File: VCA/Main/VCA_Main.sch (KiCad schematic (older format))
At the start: 35 parts, among them J1 Power, J10 IO_B, J11 IO_Power, J5 IO_A, U1 AS3360, U2 TL072, U3 TL072, U4 TL072

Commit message: Clean up VCA boards
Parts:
- added C4, C5: C, Capacitor_SMD:C_0805_2012Metric, symbol Device:C
- added R25, R26, R27, R28: R_US, Resistor_SMD:R_0805_2012Metric, symbol Device:R_US
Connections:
- net Out_A: now also R27.1, R28.1; no longer U4.1, U4.2 (-)
- net Out_B: now also R25.1, R26.1; no longer U4.6 (-), U4.7
- new net: C5.1, R27.2, U4.1
- new net: C5.2, R28.2, U4.2 (-)
- new net: C4.1, R25.2, U4.7
- new net: C4.2, R26.2, U4.6 (-)
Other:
- moved on the sheet: J1, J10, J11, J5

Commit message: Bunch of bug fixes and tweaks
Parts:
- added C6, C7, C8, C9: C, Capacitor_SMD:C_0805_2012Metric, symbol Device:C
- added H1: Top_MH1, Eurorack:eurorack_mounting_hole, symbol Mechanical:MountingHole_Pad
- added H2: Bottom_MH1, Eurorack:eurorack_mounting_hole, symbol Mechanical:MountingHole_Pad
- added H3: Top_MH2, Eurorack:eurorack_mounting_hole, symbol Mechanical:MountingHole_Pad
- added H4: Bottom_MH2, Eurorack:eurorack_mounting_hole, symbol Mechanical:MountingHole_Pad
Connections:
- net -12V: no longer J11.3 (Pin_3)
- net GNDREF: now also H1.1, H2.1, H3.1, H4.1
- net at R10.2, R8.1, U3.1: now also C7.1
- net at R4.1, R5.1, R6.1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: now also C7.2
- net at R10.1, R12.2, U3.6 (-): now also C9.2
- net at R12.1, R15.1, U3.7: now also C9.1
- net at R7.1, R9.2, U2.1: now also C6.1
- net at R1.1, R2.1, R3.1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: now also C6.2
- net at R11.2, R9.1, U2.6 (-): now also C8.2
- net at R11.1, R13.1, U2.7: now also C8.1
- no-connect marks 0 -> 1
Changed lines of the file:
@@
 	10500 3550 10600 3550
-Wire Wire Line
-	10550 2950 10250 2950
-Wire Wire Line
-	10250 2950 10250 3250
-$Comp
-L power:-12V #PWR0105
-U 1 1 5D8742CF
-P 10250 3250
-F 0 "#PWR0105" H 10250 3350 50  0001 C CNN
-F 1 "-12V" H 10265 3423 50  0000 C CNN
-F 2 "" H 10250 3250 50  0001 C CNN
-F 3 "" H 10250 3250 50  0001 C CNN
-	1    10250 3250
-	-1   0    0    1
-$EndComp
 Wire Wire Line
 	9750 5150 10600 5150
@@
 	8700 5500 8800 5500
 Connection ~ 8700 5500
+$Comp
+L Device:C C6
+U 1 1 5D936AAB
+P 2400 2450
+F 0 "C6" V 2148 2450 50  0000 C CNN
+F 1 "C" V 2239 2450 50  0000 C CNN
+F 2 "Capacitor_SMD:C_0805_2012Metric" H 2438 2300 50  0001 C CNN
+F 3 "~" H 2400 2450 50  0001 C CNN
+	1    2400 2450
+	0    1    1    0
+$EndComp
+Wire Wire Line
+	2550 2450 2800 2450
+Wire Wire Line
+	2800 2450 2800 2000
+Connection ~ 2800 2000
+Wire Wire Line
+	2250 2450 2000 2450
+Wire Wire Line
+	2000 2450 2000 2000
+Connection ~ 2000 2000
+$Comp
+L Device:C C8
+U 1 1 5D94AAF9
+P 3700 2350
+F 0 "C8" V 3448 2350 50  0000 C CNN
+F 1 "C" V 3539 2350 50  0000 C CNN
+F 2 "Capacitor_SMD:C_0805_2012Metric" H 3738 2200 50  0001 C CNN
+F 3 "~" H 3700 2350 50  0001 C CNN
+	1    3700 2350
+	0    1    1    0
+$EndComp
+Wire Wire Line
+	3550 2350 3300 2350
+Wire Wire Line
+	3300 2350 3300 1900
+Connection ~ 3300 1900
+Wire Wire Line
+	3850 2350 4100 2350
+Wire Wire Line
+	4100 2350 4100 1900
+Connection ~ 4100 1900
+$Comp
+L Device:C C7
+U 1 1 5D960DB1
+P 2400 5550
+F 0 "C7" V 2148 5550 50  0000 C CNN
+F 1 "C" V 2239 5550 50  0000 C CNN
+F 2 "Capacitor_SMD:C_0805_2012Metric" H 2438 5400 50  0001 C CNN
+F 3 "~" H 2400 5550 50  0001 C CNN
+	1    2400 5550
+	0    1    1    0
+$EndComp
+Wire Wire Line
+	2000 5100 2000 5550
+Wire Wire Line
+	2000 5550 2250 5550
+Connection ~ 2000 5100
+Wire Wire Line
+	2800 5100 2800 5550
+Wire Wire Line
+	2800 5550 2550 5550
+Connection ~ 2800 5100
+$Comp
+L Device:C C9
+U 1 1 5D9785AA
+P 3700 5450
+F 0 "C9" V 3448 5450 50  0000 C CNN
+F 1 "C" V 3539 5450 50  0000 C CNN
+F 2 "Capacitor_SMD:C_0805_2012Metric" H 3738 5300 50  0001 C CNN
+F 3 "~" H 3700 5450 50  0001 C CNN
+	1    3700 5450
+	0    1    1    0
+$EndComp
+Wire Wire Line
+	3300 5000 3300 5450
+Wire Wire Line
+	3300 5450 3550 5450
+Connection ~ 3300 5000
+Wire Wire Line
+	3850 5450 4100 5450
+Wire Wire Line
+	4100 5450 4100 5000
+Connection ~ 4100 5000
+$Comp
+L Mechanical:MountingHole_Pad H1
+U 1 1 5D996C4A
+P 7650 800
+F 0 "H1" H 7750 849 50  0000 L CNN
+F 1 "Top_MH1" H 7750 758 50  0000 L CNN
+F 2 "Eurorack:eurorack_mounting_hole" H 7650 800 50  0001 C CNN
+F 3 "~" H 7650 800 50  0001 C CNN
+	1    7650 800
+	1    0    0    -1
+$EndComp
+$Comp
+L power:GNDREF #PWR0133
+U 1 1 5D997D60
+P 7650 900
+F 0 "#PWR0133" H 7650 650 50  0001 C CNN
+F 1 "GNDREF" H 7655 727 50  0001 C CNN
+F 2 "" H 7650 900 50  0001 C CNN
+F 3 "" H 7650 900 50  0001 C CNN
+	1    7650 900
+	1    0    0    -1
+$EndComp
+$Comp
+L Mechanical:MountingHole_Pad H3
+U 1 1 5D999222
+P 8500 800
+F 0 "H3" H 8600 849 50  0000 L CNN
+F 1 "Top_MH2" H 8600 758 50  0000 L CNN
+F 2 "Eurorack:eurorack_mounting_hole" H 8500 800 50  0001 C CNN
+F 3 "~" H 8500 800 50  0001 C CNN
+	1    8500 800
+	1    0    0    -1
+$EndComp
+$Comp
+L power:GNDREF #PWR0134
+U 1 1 5D999228
+P 8500 900
+F 0 "#PWR0134" H 8500 650 50  0001 C CNN
+F 1 "GNDREF" H 8505 727 50  0001 C CNN
+F 2 "" H 8500 900 50  0001 C CNN
+F 3 "" H 8500 900 50  0001 C CNN
+	1    8500 900
+	1    0    0    -1
+$EndComp
+$Comp
+L Mechanical:MountingHole_Pad H2
+U 1 1 5D9A4134
+P 7650 1200
+F 0 "H2" H 7750 1249 50  0000 L CNN
+F 1 "Bottom_MH1" H 7750 1158 50  0000 L CNN
+F 2 "Eurorack:eurorack_mounting_hole" H 7650 1200 50  0001 C CNN
+F 3 "~" H 7650 1200 50  0001 C CNN
+	1    7650 1200
+	1    0    0    -1
+$EndComp
+$Comp
+L power:GNDREF #PWR0135
+U 1 1 5D9A413A
+P 7650 1300
+F 0 "#PWR0135" H 7650 1050 50  0001 C CNN
+F 1 "GNDREF" H 7655 1127 50  0001 C CNN
+F 2 "" H 7650 1300 50  0001 C CNN
+F 3 "" H 7650 1300 50  0001 C CNN
+	1    7650 1300
+	1    0    0    -1
+$EndComp
+$Comp
+L Mechanical:MountingHole_Pad H4
+U 1 1 5D9AEFCE
+P 8500 1200
+F 0 "H4" H 8600 1249 50  0000 L CNN
+F 1 "Bottom_MH2" H 8600 1158 50  0000 L CNN
+F 2 "Eurorack:eurorack_mounting_hole" H 8500 1200 50  0001 C CNN
+F 3 "~" H 8500 1200 50  0001 C CNN
+	1    8500 1200
+	1    0    0    -1
+$EndComp
+$Comp
+L power:GNDREF #PWR0136
+U 1 1 5D9AEFD4
+P 8500 1300
+F 0 "#PWR0136" H 8500 1050 50  0001 C CNN
+F 1 "GNDREF" H 8505 1127 50  0001 C CNN
+F 2 "" H 8500 1300 50  0001 C CNN
+F 3 "" H 8500 1300 50  0001 C CNN
+	1    8500 1300
+	1    0    0    -1
+$EndComp
+NoConn ~ 10550 2950
 $EndSCHEMATC

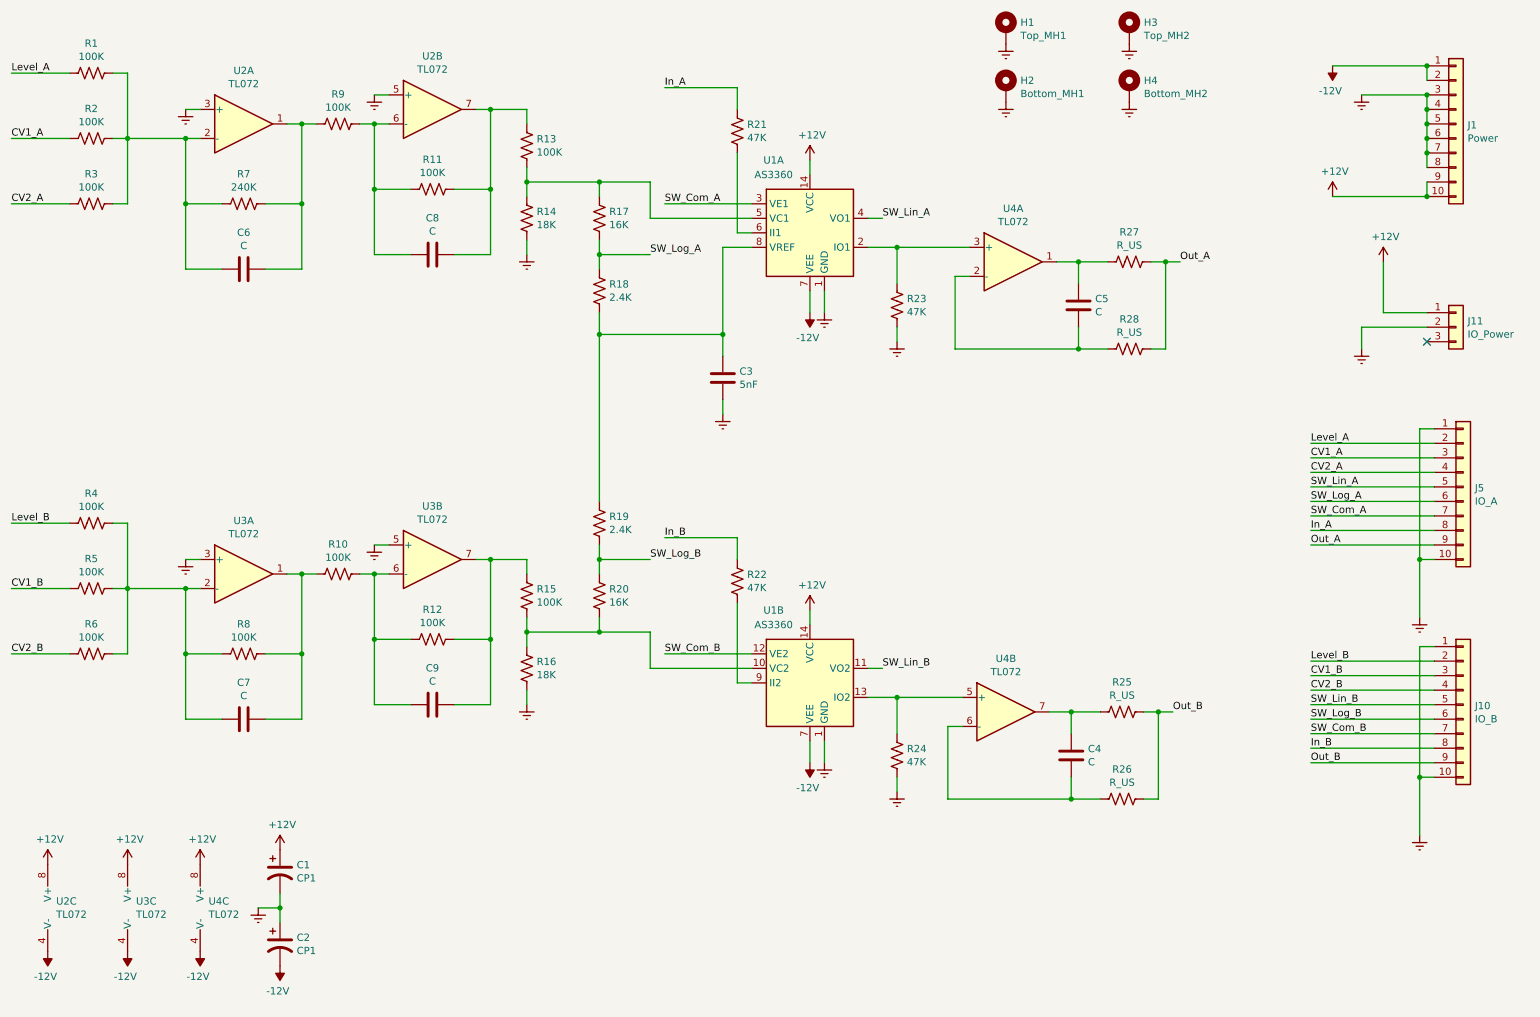
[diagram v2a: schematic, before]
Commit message: Clean up layout of VCA board
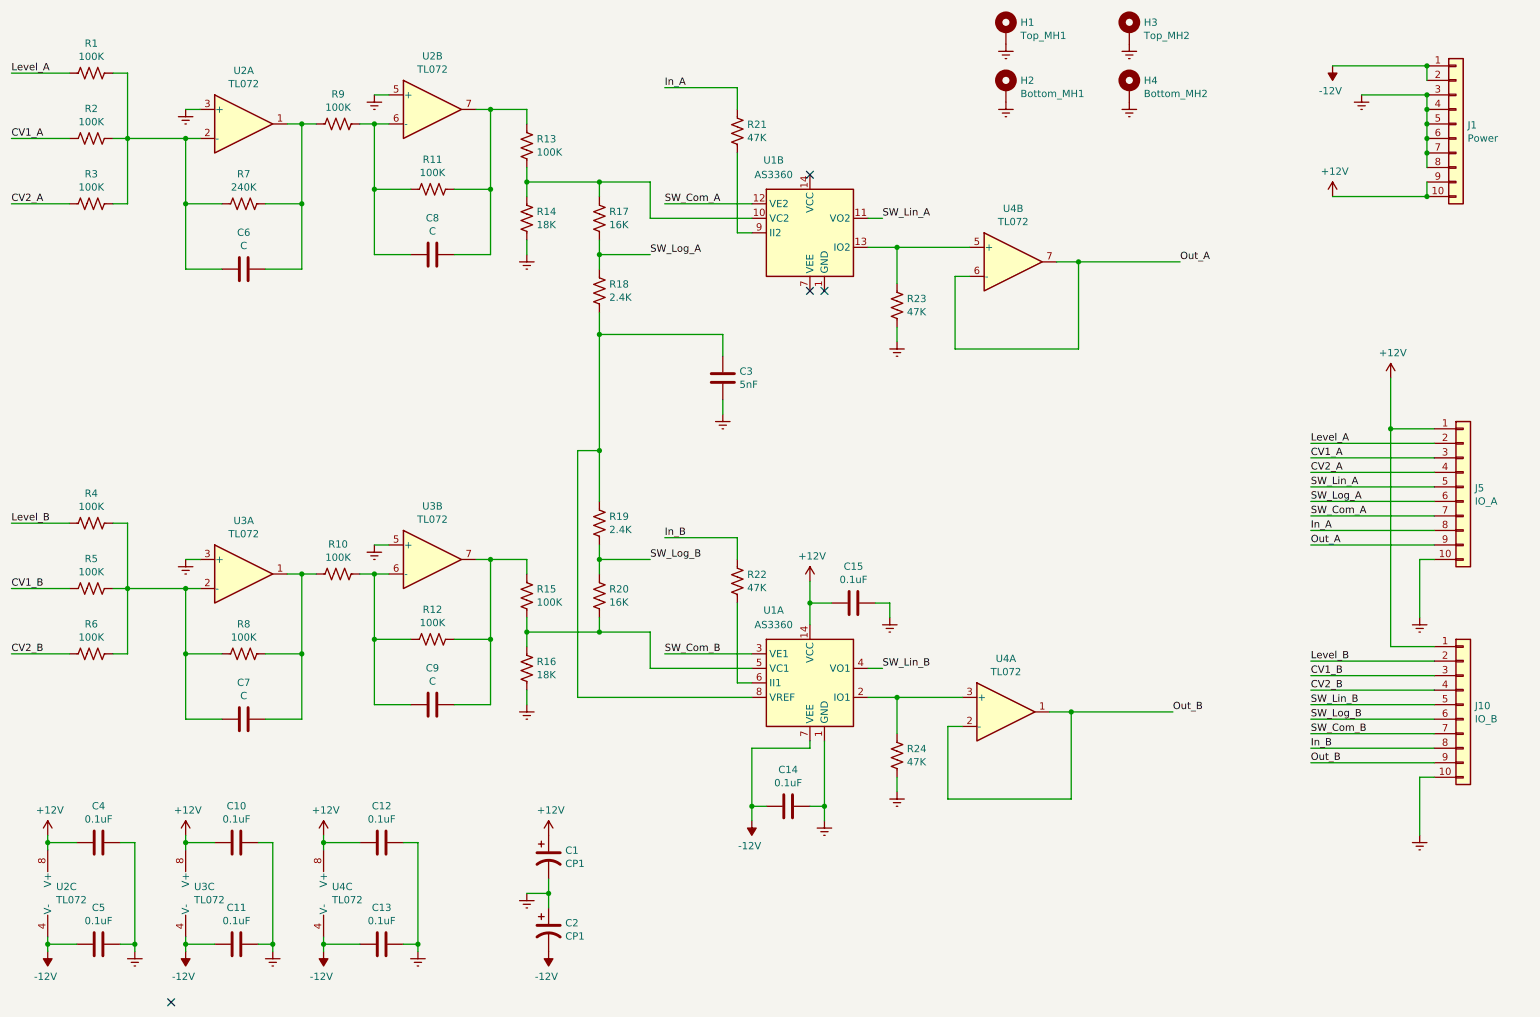
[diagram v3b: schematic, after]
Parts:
- removed J11: IO_Power, Connector_PinHeader_2.54mm:PinHeader_1x03_P2.54mm_Vertical, symbol Connector_Generic:Conn_01x03
- removed R25, R26, R27, R28: R_US, Resistor_SMD:R_0805_2012Metric, symbol Device:R_US
- added C10, C11, C12, C13, C14, C15: 0.1uF, Capacitor_SMD:C_0805_2012Metric, symbol Device:C
- C4, C5: value C -> 0.1uF
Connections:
- net +12V: now also C4.2, J10.1 (Pin_1), J5.1 (Pin_1), C10.2, C12.2, C15.2; no longer U1.14 (VCC)
- net -12V: now also C5.2, C11.2, C13.2, C14.2; no longer U1.7 (VEE)
- net GNDREF: now also C4.1, C5.1, C10.1, C11.1, C12.1, C13.1, C14.1, C15.1; no longer J10.1 (Pin_1), J5.1 (Pin_1), U1.1 (GND)
- net Out_A: now also U4.6 (-), U4.7
- net Out_B: now also U4.1, U4.2 (-)
- net SW_Com_A: now also U1.12 (VE2); no longer U1.3 (VE1)
- net SW_Com_B: now also U1.3 (VE1); no longer U1.12 (VE2)
- net SW_Lin_A: now also U1.11 (VO2); no longer U1.4 (VO1)
- net SW_Lin_B: now also U1.4 (VO1); no longer U1.11 (VO2)
- net at R15.2, R16.1, R20.2: now also U1.5 (VC1); no longer U1.10 (VC2)
- net at U1.2 (IO1), U4.3 (+): now also R24.1; no longer R23.1
- net at R13.2, R14.1, R17.1: now also U1.10 (VC2); no longer U1.5 (VC1)
- net at U1.6 (II1): now also R22.2; no longer R21.2
- net at U1.13 (IO2), U4.5 (+): now also R23.1; no longer R24.1
- net at U1.9 (II2): now also R21.2; no longer R22.2
- no-connect marks 1 -> 4
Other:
- moved on the sheet: C1, C2, U1A, U1B, U2C, U3C, U4A, U4B, U4C
